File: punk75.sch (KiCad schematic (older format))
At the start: 190 parts, among them J1 AVR-ISP-6, SW1 RESET, SW2 BOOT, U1 ATmega32A-PU, Y1 16MHz

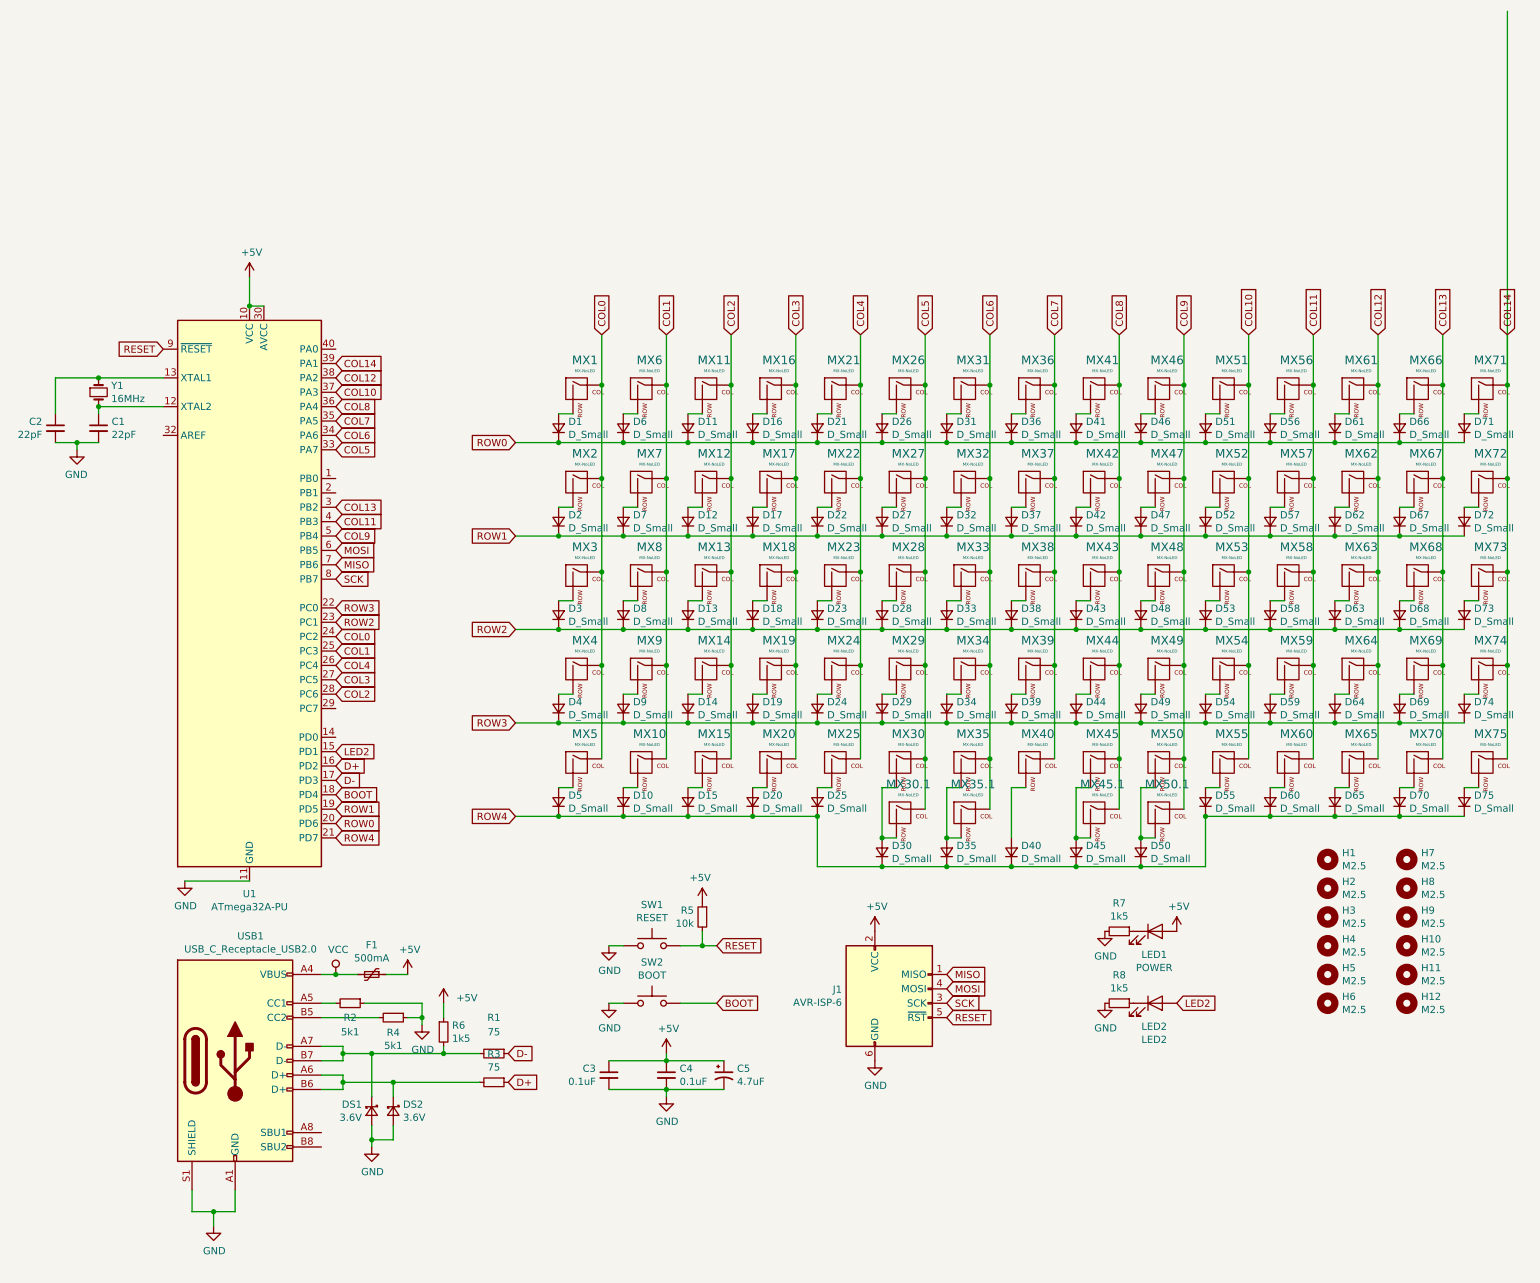
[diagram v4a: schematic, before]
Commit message: added 2 rotary encoders and changed some traces to use them
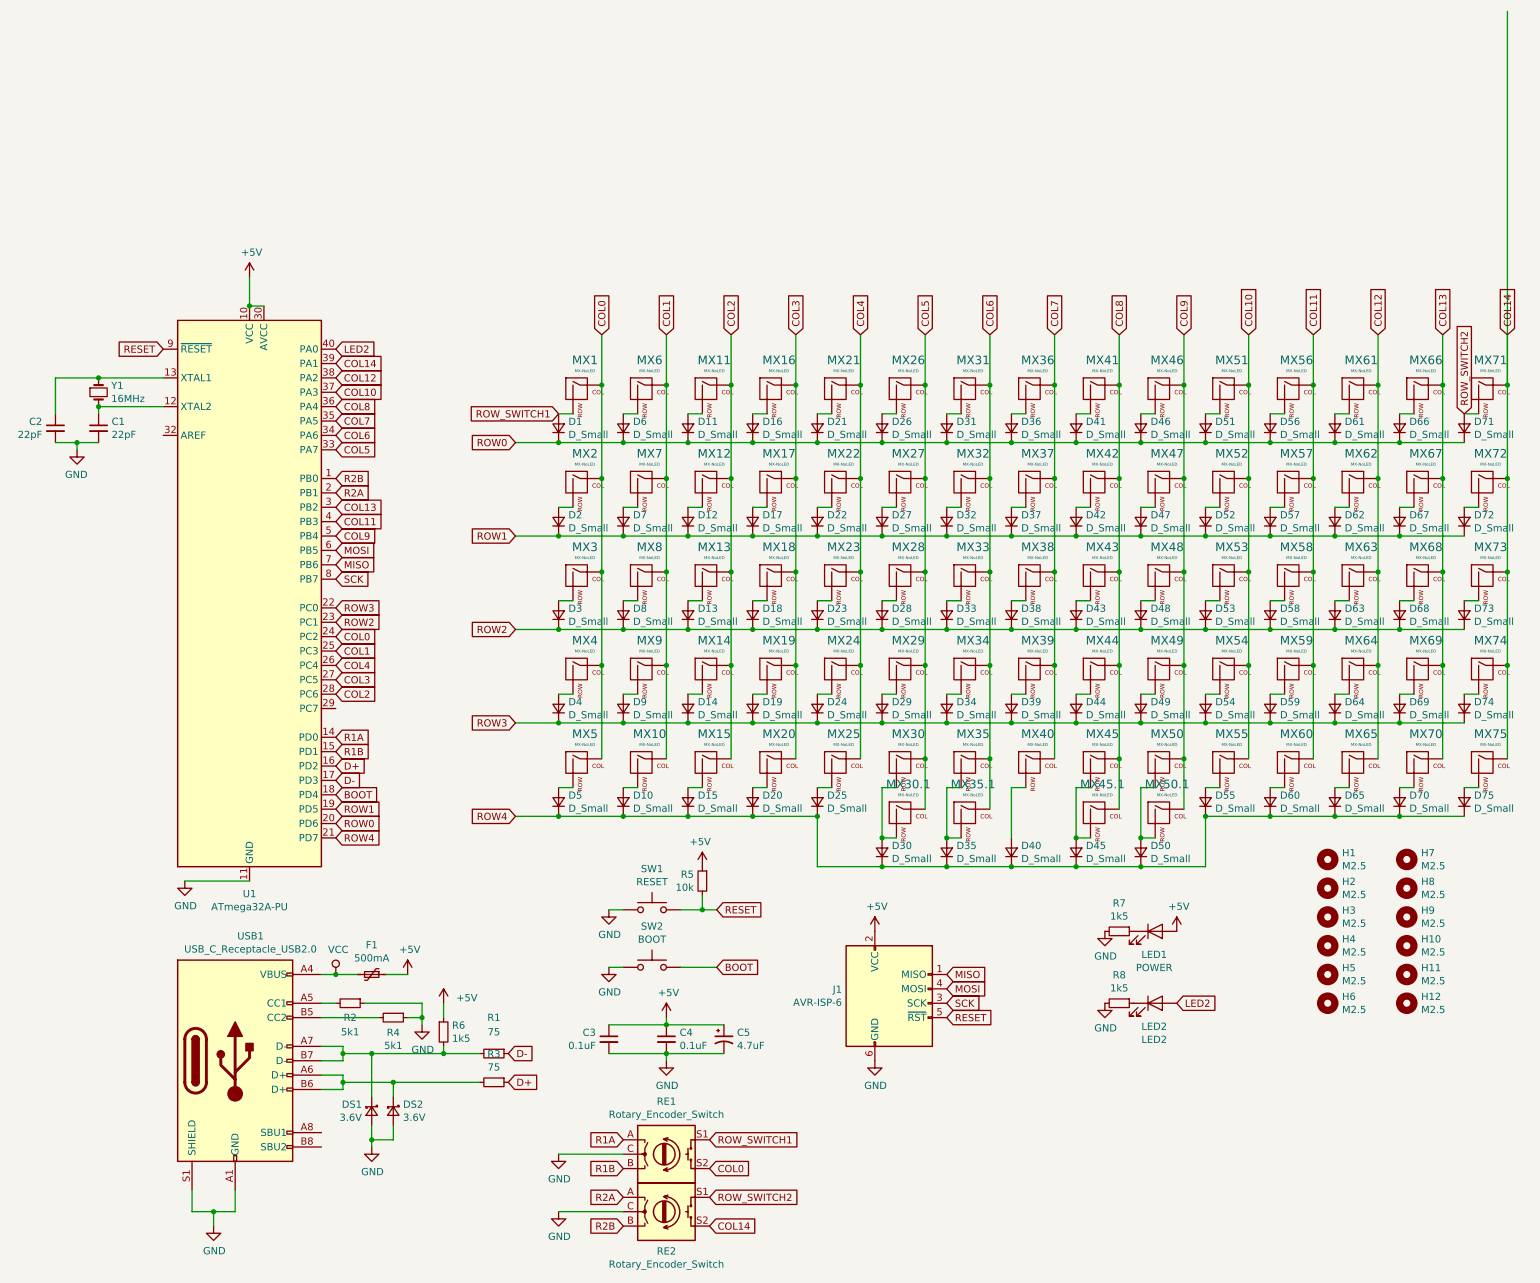
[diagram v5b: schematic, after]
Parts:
- added RE1, RE2: Rotary_Encoder_Switch, Rotary_Encoder:RotaryEncoder_Alps_EC11E-Switch_Vertical_H20mm_CircularMountingHoles, symbol Device:Rotary_Encoder_Switch
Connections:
- net COL0: now also RE1.S2
- net COL14: now also RE2.S2
- net GND: now also RE1.C, RE2.C
- net LED2: now also U1.40 (PA0); no longer U1.15 (PD1)
- net ROW_SWITCH1: now reaches D1.2 (A), MX1.2 (ROW)
- net ROW_SWITCH1: now also RE1.S1
- net R2B: now reaches U1.1 (PB0)
- net R2B: now also RE2.B
- net R1A: now reaches U1.14 (PD0)
- net R1A: now also RE1.A
- net R2A: now reaches U1.2 (PB1)
- net R2A: now also RE2.A
- net ROW_SWITCH2: now reaches D71.2 (A), MX71.2 (ROW)
- net ROW_SWITCH2: now also RE2.S1
- new net R1B: RE1.B, U1.15 (PD1)
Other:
- moved on the sheet: C3, C4, C5, R5, SW1, SW2
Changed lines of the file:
@@
 L Device:C_Small C4
 U 1 1 5E99FFDC
-P 5100 6400
-F 0 "C4" H 5192 6446 50  0000 L CNN
-F 1 "0.1uF" H 5192 6355 50  0000 L CNN
-F 2 "Capacitor_THT:C_Disc_D4.3mm_W1.9mm_P5.00mm" H 5100 6400 50  0001 C CNN
-F 3 "~" H 5100 6400 50  0001 C CNN
-	1    5100 6400
+P 5100 6150
+F 0 "C4" H 5192 6196 50  0000 L CNN
+F 1 "0.1uF" H 5192 6105 50  0000 L CNN
+F 2 "Capacitor_THT:C_Disc_D4.3mm_W1.9mm_P5.00mm" H 5100 6150 50  0001 C CNN
+F 3 "~" H 5100 6150 50  0001 C CNN
+	1    5100 6150
 	1    0    0    -1
 $EndComp
@@
 L Device:CP1_Small C5
 U 1 1 5E9A0A50
-P 5500 6400
-F 0 "C5" H 5591 6446 50  0000 L CNN
-F 1 "4.7uF" H 5591 6355 50  0000 L CNN
-F 2 "Capacitor_THT:CP_Radial_D4.0mm_P1.50mm" H 5500 6400 50  0001 C CNN
-F 3 "~" H 5500 6400 50  0001 C CNN
-	1    5500 6400
+P 5500 6150
+F 0 "C5" H 5591 6196 50  0000 L CNN
+F 1 "4.7uF" H 5591 6105 50  0000 L CNN
+F 2 "Capacitor_THT:CP_Radial_D4.0mm_P1.50mm" H 5500 6150 50  0001 C CNN
+F 3 "~" H 5500 6150 50  0001 C CNN
+	1    5500 6150
 	1    0    0    -1
 $EndComp
@@
 L power:+5V #PWR0102
 U 1 1 5E9A1278
-P 5100 6250
-F 0 "#PWR0102" H 5100 6100 50  0001 C CNN
-F 1 "+5V" H 5115 6423 50  0000 C CNN
-F 2 "" H 5100 6250 50  0001 C CNN
-F 3 "" H 5100 6250 50  0001 C CNN
-	1    5100 6250
+P 5100 6000
+F 0 "#PWR0102" H 5100 5850 50  0001 C CNN
+F 1 "+5V" H 5115 6173 50  0000 C CNN
+F 2 "" H 5100 6000 50  0001 C CNN
+F 3 "" H 5100 6000 50  0001 C CNN
+	1    5100 6000
 	1    0    0    -1
 $EndComp
@@
 L power:GND #PWR0103
 U 1 1 5E9A1A45
-P 5100 6550
-F 0 "#PWR0103" H 5100 6300 50  0001 C CNN
-F 1 "GND" H 5105 6377 50  0000 C CNN
-F 2 "" H 5100 6550 50  0001 C CNN
-F 3 "" H 5100 6550 50  0001 C CNN
-	1    5100 6550
+P 5100 6300
+F 0 "#PWR0103" H 5100 6050 50  0001 C CNN
+F 1 "GND" H 5105 6127 50  0000 C CNN
+F 2 "" H 5100 6300 50  0001 C CNN
+F 3 "" H 5100 6300 50  0001 C CNN
+	1    5100 6300
 	1    0    0    -1
 $EndComp
 Wire Wire Line
-	5100 6500 5100 6550
-Connection ~ 5100 6500
+	5100 6250 5100 6300
+Connection ~ 5100 6250
 Wire Wire Line
-	5100 6500 5500 6500
+	5100 6250 5500 6250
 Wire Wire Line
-	5100 6250 5100 6300
-Connection ~ 5100 6300
+	5100 6000 5100 6050
+Connection ~ 5100 6050
 Wire Wire Line
-	5100 6300 5500 6300
+	5100 6050 5500 6050
 $Comp
 L Device:C_Small C2
@@
 L Switch:SW_Push SW1
 U 1 1 5E9AF7FA
-P 5000 5500
-F 0 "SW1" H 5000 5785 50  0000 C CNN
-F 1 "RESET" H 5000 5694 50  0000 C CNN
-F 2 "Button_Switch_THT:SW_PUSH_6mm" H 5000 5700 50  0001 C CNN
-F 3 "~" H 5000 5700 50  0001 C CNN
-	1    5000 5500
+P 5000 5250
+F 0 "SW1" H 5000 5535 50  0000 C CNN
+F 1 "RESET" H 5000 5444 50  0000 C CNN
+F 2 "Button_Switch_THT:SW_PUSH_6mm" H 5000 5450 50  0001 C CNN
+F 3 "~" H 5000 5450 50  0001 C CNN
+	1    5000 5250
 	-1   0    0    -1
 $EndComp
 Wire Wire Line
-	5200 5500 5350 5500
+	5200 5250 5350 5250
 $Comp
 L Device:R_Small R5
 U 1 1 5E9B0DD7
-P 5350 5300
-F 0 "R5" H 5409 5346 50  0000 L CNN
-F 1 "10k" H 5409 5255 50  0000 L CNN
-F 2 "Resistor_THT:R_Axial_DIN0204_L3.6mm_D1.6mm_P5.08mm_Horizontal" H 5350 5300 50  0001 C CNN
-F 3 "~" H 5350 5300 50  0001 C CNN
-	1    5350 5300
+P 5350 5050
+F 0 "R5" H 5409 5096 50  0000 L CNN
+F 1 "10k" H 5409 5005 50  0000 L CNN
+F 2 "Resistor_THT:R_Axial_DIN0204_L3.6mm_D1.6mm_P5.08mm_Horizontal" H 5350 5050 50  0001 C CNN
+F 3 "~" H 5350 5050 50  0001 C CNN
+	1    5350 5050
 	-1   0    0    -1
 $EndComp
-Connection ~ 5350 5500
+Connection ~ 5350 5250
 Wire Wire Line
-	5450 5500 5350 5500
+	5450 5250 5350 5250
 Wire Wire Line
-	5350 5400 5350 5500
+	5350 5150 5350 5250
 $Comp
 L power:+5V #PWR0107
 U 1 1 5E9B9DA9
-P 5350 5200
-F 0 "#PWR0107" H 5350 5050 50  0001 C CNN
-F 1 "+5V" H 5365 5373 50  0000 C CNN
-F 2 "" H 5350 5200 50  0001 C CNN
-F 3 "" H 5350 5200 50  0001 C CNN
-	1    5350 5200
+P 5350 4950
+F 0 "#PWR0107" H 5350 4800 50  0001 C CNN
+F 1 "+5V" H 5365 5123 50  0000 C CNN
+F 2 "" H 5350 4950 50  0001 C CNN
+F 3 "" H 5350 4950 50  0001 C CNN
+	1    5350 4950
 	-1   0    0    -1
 $EndComp
@@
 L Switch:SW_Push SW2
 U 1 1 5E9DAEA9
-P 5000 5900
-F 0 "SW2" H 5000 6185 50  0000 C CNN
-F 1 "BOOT" H 5000 6094 50  0000 C CNN
-F 2 "Button_Switch_THT:SW_PUSH_6mm" H 5000 6100 50  0001 C CNN
-F 3 "~" H 5000 6100 50  0001 C CNN
-	1    5000 5900
+P 5000 5650
+F 0 "SW2" H 5000 5935 50  0000 C CNN
+F 1 "BOOT" H 5000 5844 50  0000 C CNN
+F 2 "Button_Switch_THT:SW_PUSH_6mm" H 5000 5850 50  0001 C CNN
+F 3 "~" H 5000 5850 50  0001 C CNN
+	1    5000 5650
 	1    0    0    -1
 $EndComp
@@
 L Device:C_Small C3
 U 1 1 5E9E1C12
-P 4700 6400
-F 0 "C3" H 4609 6446 50  0000 R CNN
-F 1 "0.1uF" H 4609 6355 50  0000 R CNN
-F 2 "Capacitor_THT:C_Disc_D4.3mm_W1.9mm_P5.00mm" H 4700 6400 50  0001 C CNN
-F 3 "~" H 4700 6400 50  0001 C CNN
-	1    4700 6400
+P 4700 6150
+F 0 "C3" H 4609 6196 50  0000 R CNN
+F 1 "0.1uF" H 4609 6105 50  0000 R CNN
+F 2 "Capacitor_THT:C_Disc_D4.3mm_W1.9mm_P5.00mm" H 4700 6150 50  0001 C CNN
+F 3 "~" H 4700 6150 50  0001 C CNN
+	1    4700 6150
 	1    0    0    -1
 $EndComp
 Wire Wire Line
-	5100 6300 4700 6300
+	5100 6050 4700 6050
 Wire Wire Line
-	5100 6500 4700 6500
+	5100 6250 4700 6250
 $Comp
 L Connector:USB_C_Receptacle_USB2.0 USB1
@@
 L power:GND #PWR0114
 U 1 1 5EC768AD
-P 4700 5500
-F 0 "#PWR0114" H 4700 5250 50  0001 C CNN
-F 1 "GND" H 4705 5327 50  0000 C CNN
-F 2 "" H 4700 5500 50  0001 C CNN
-F 3 "" H 4700 5500 50  0001 C CNN
-	1    4700 5500
+P 4700 5250
+F 0 "#PWR0114" H 4700 5000 50  0001 C CNN
+F 1 "GND" H 4705 5077 50  0000 C CNN
+F 2 "" H 4700 5250 50  0001 C CNN
+F 3 "" H 4700 5250 50  0001 C CNN
+	1    4700 5250
 	1    0    0    -1
 $EndComp
 Wire Wire Line
-	4700 5500 4800 5500
+	4700 5250 4800 5250
 Connection ~ 4650 1600
 $Comp
@@
 	1    0    0    -1
 $EndComp
-Text GLabel 5450 5500 2    50   Input ~ 0
+Text GLabel 5450 5250 2    50   Input ~ 0
 RESET
 Text GLabel 1600 1350 0    50   Input ~ 0
@@
 L power:GND #PWR0116
 U 1 1 5ECCE6CC
-P 4700 5900
-F 0 "#PWR0116" H 4700 5650 50  0001 C CNN
-F 1 "GND" H 4705 5727 50  0000 C CNN
-F 2 "" H 4700 5900 50  0001 C CNN
-F 3 "" H 4700 5900 50  0001 C CNN
-	1    4700 5900
+P 4700 5650
+F 0 "#PWR0116" H 4700 5400 50  0001 C CNN
+F 1 "GND" H 4705 5477 50  0000 C CNN
+F 2 "" H 4700 5650 50  0001 C CNN
+F 3 "" H 4700 5650 50  0001 C CNN
+	1    4700 5650
 	1    0    0    -1
 $EndComp
 Wire Wire Line
-	4800 5900 4700 5900
-Text GLabel 5450 5900 2    50   Input ~ 0
+	4800 5650 4700 5650
+Text GLabel 5450 5650 2    50   Input ~ 0
 BOOT
 Wire Wire Line
-	5450 5900 5200 5900
+	5450 5650 5200 5650
 Text GLabel 2800 4450 2    50   Input ~ 0
 BOOT
@@
 Text GLabel 8650 5900 2    50   Input ~ 0
 LED2
-Text GLabel 2800 4150 2    50   Input ~ 0
+Text GLabel 2800 1350 2    50   Input ~ 0
 LED2
+$Comp
+L Device:Rotary_Encoder_Switch RE1
+U 1 1 5EC58FA9
+P 5100 6950
+F 0 "RE1" H 5100 7317 50  0000 C CNN
+F 1 "Rotary_Encoder_Switch" H 5100 7226 50  0000 C CNN
+F 2 "Rotary_Encoder:RotaryEncoder_Alps_EC11E-Switch_Vertical_H20mm_CircularMountingHoles" H 4950 7110 50  0001 C CNN
+F 3 "~" H 5100 7210 50  0001 C CNN
+	1    5100 6950
+	1    0    0    -1
+$EndComp
+$Comp
+L Device:Rotary_Encoder_Switch RE2
+U 1 1 5EC5E50D
+P 5100 7350
+F 0 "RE2" H 5100 7075 50  0000 C CNN
+F 1 "Rotary_Encoder_Switch" H 5100 6984 50  0000 C CNN
+F 2 "Rotary_Encoder:RotaryEncoder_Alps_EC11E-Switch_Vertical_H20mm_CircularMountingHoles" H 4950 7510 50  0001 C CNN
+F 3 "~" H 5100 7610 50  0001 C CNN
+	1    5100 7350
+	1    0    0    -1
+$EndComp
+Text GLabel 4350 1800 0    50   Input ~ 0
+ROW_SWITCH1
+Text GLabel 10650 1800 1    50   Input ~ 0
+ROW_SWITCH2
+Text GLabel 5400 6850 2    50   Input ~ 0
+ROW_SWITCH1
+Text GLabel 5400 7050 2    50   Input ~ 0
+COL0
+Text GLabel 5400 7250 2    50   Input ~ 0
+ROW_SWITCH2
+Text GLabel 5400 7450 2    50   Input ~ 0
+COL14
+$Comp
+L power:GND #PWR0120
+U 1 1 5ED71FD4
+P 4350 6950
+F 0 "#PWR0120" H 4350 6700 50  0001 C CNN
+F 1 "GND" H 4355 6777 50  0000 C CNN
+F 2 "" H 4350 6950 50  0001 C CNN
+F 3 "" H 4350 6950 50  0001 C CNN
+	1    4350 6950
+	1    0    0    -1
+$EndComp
+$Comp
+L power:GND #PWR0121
+U 1 1 5ED727DD
+P 4350 7350
+F 0 "#PWR0121" H 4350 7100 50  0001 C CNN
+F 1 "GND" H 4355 7177 50  0000 C CNN
+F 2 "" H 4350 7350 50  0001 C CNN
+F 3 "" H 4350 7350 50  0001 C CNN
+	1    4350 7350
+	1    0    0    -1
+$EndComp
+Wire Wire Line
+	4350 7350 4800 7350
+Wire Wire Line
+	4800 6950 4350 6950
+Text GLabel 4800 6850 0    50   Input ~ 0
+R1A
+Text GLabel 4800 7050 0    50   Input ~ 0
+R1B
+Text GLabel 4800 7450 0    50   Input ~ 0
+R2B
+Text GLabel 4800 7250 0    50   Input ~ 0
+R2A
+Text GLabel 2800 4050 2    50   Input ~ 0
+R1A
+Text GLabel 2800 4150 2    50   Input ~ 0
+R1B
+Text GLabel 2800 2350 2    50   Input ~ 0
+R2A
+Text GLabel 2800 2250 2    50   Input ~ 0
+R2B
 $EndSCHEMATC

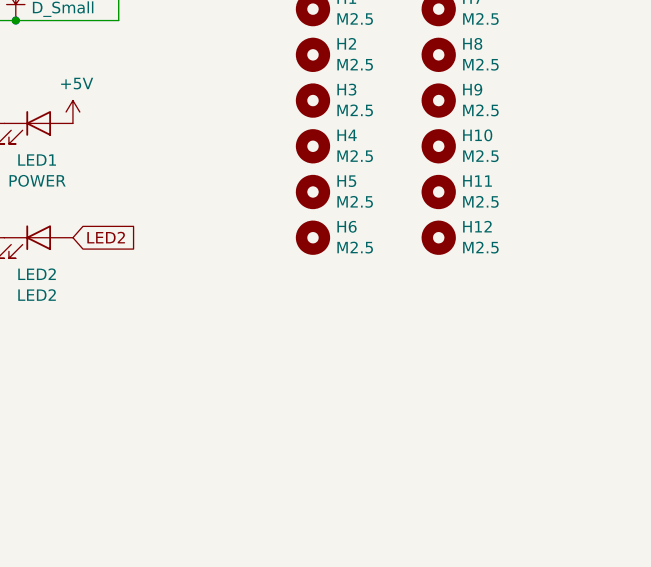
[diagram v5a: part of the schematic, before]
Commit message: added two more mounting holes and moved other two
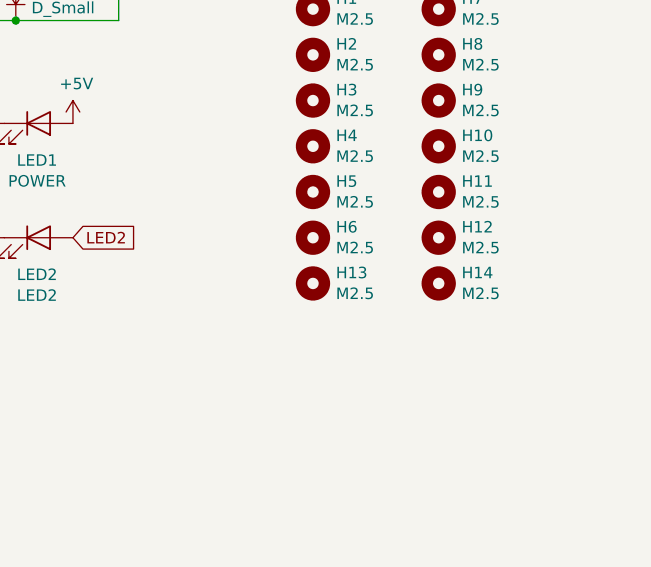
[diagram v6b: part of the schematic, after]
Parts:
- added H13, H14: M2.5, MountingHole:MountingHole_2.7mm_M2.5_ISO7380_Pad, symbol Mechanical:MountingHole
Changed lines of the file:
@@
 Text GLabel 2800 2250 2    50   Input ~ 0
 R2B
+$Comp
+L Mechanical:MountingHole H13
+U 1 1 5EC747DD
+P 9700 6100
+F 0 "H13" H 9800 6146 50  0000 L CNN
+F 1 "M2.5" H 9800 6055 50  0000 L CNN
+F 2 "MountingHole:MountingHole_2.7mm_M2.5_ISO7380_Pad" H 9700 6100 50  0001 C CNN
+F 3 "~" H 9700 6100 50  0001 C CNN
+	1    9700 6100
+	1    0    0    -1
+$EndComp
+$Comp
+L Mechanical:MountingHole H14
+U 1 1 5EC747E7
+P 10250 6100
+F 0 "H14" H 10350 6146 50  0000 L CNN
+F 1 "M2.5" H 10350 6055 50  0000 L CNN
+F 2 "MountingHole:MountingHole_2.7mm_M2.5_ISO7380_Pad" H 10250 6100 50  0001 C CNN
+F 3 "~" H 10250 6100 50  0001 C CNN
+	1    10250 6100
+	1    0    0    -1
+$EndComp
 $EndSCHEMATC
